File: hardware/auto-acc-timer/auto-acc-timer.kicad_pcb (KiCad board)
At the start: 2 copper layers, 38.1 x 20.3 mm, 12 parts, among them J1 Conn_01x07_Pin, J3 Conn_02x03_Odd_Even, Q1 BRC108, Q2 BSS83P, U1 ATtiny85-20S, U2 MCP1703Ax-330xxDB

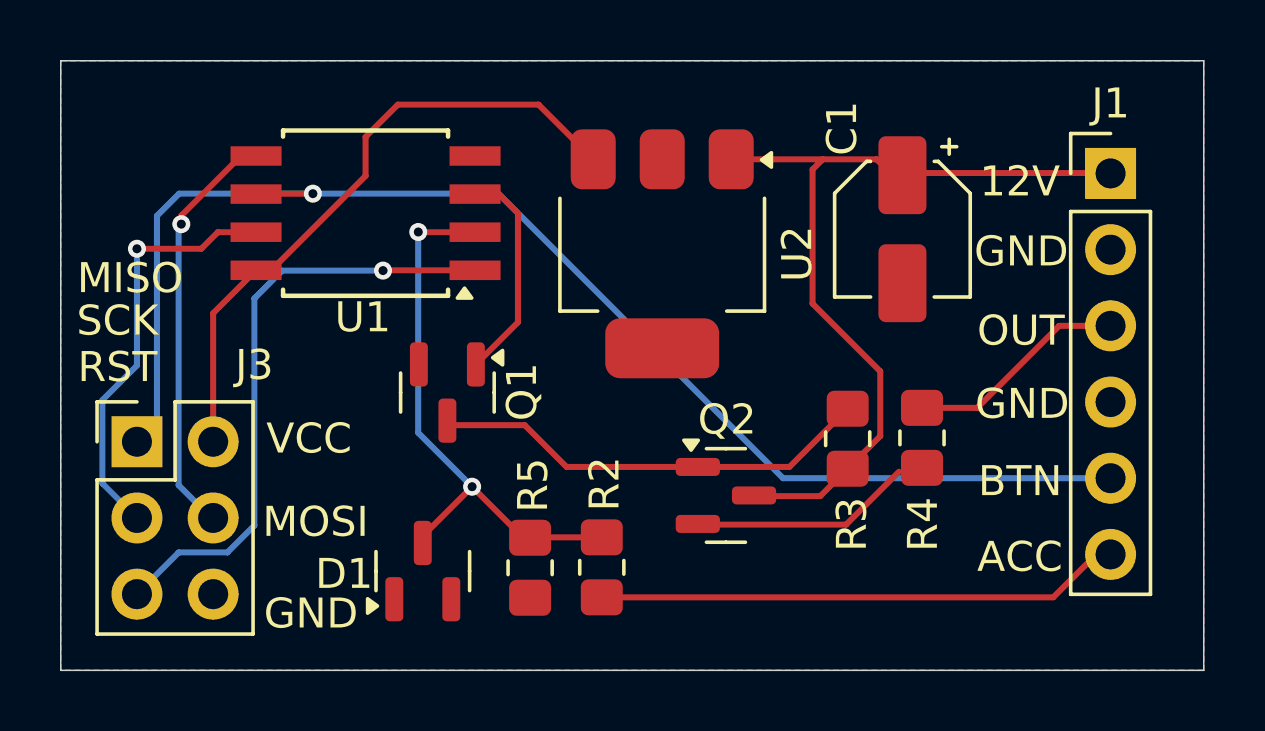
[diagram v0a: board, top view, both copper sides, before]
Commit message: Fix wrong connection of Q2, move to KiCAD v 9
The Q2 FET was connected the wrong way, fix that. and Move to KiCAD
version9
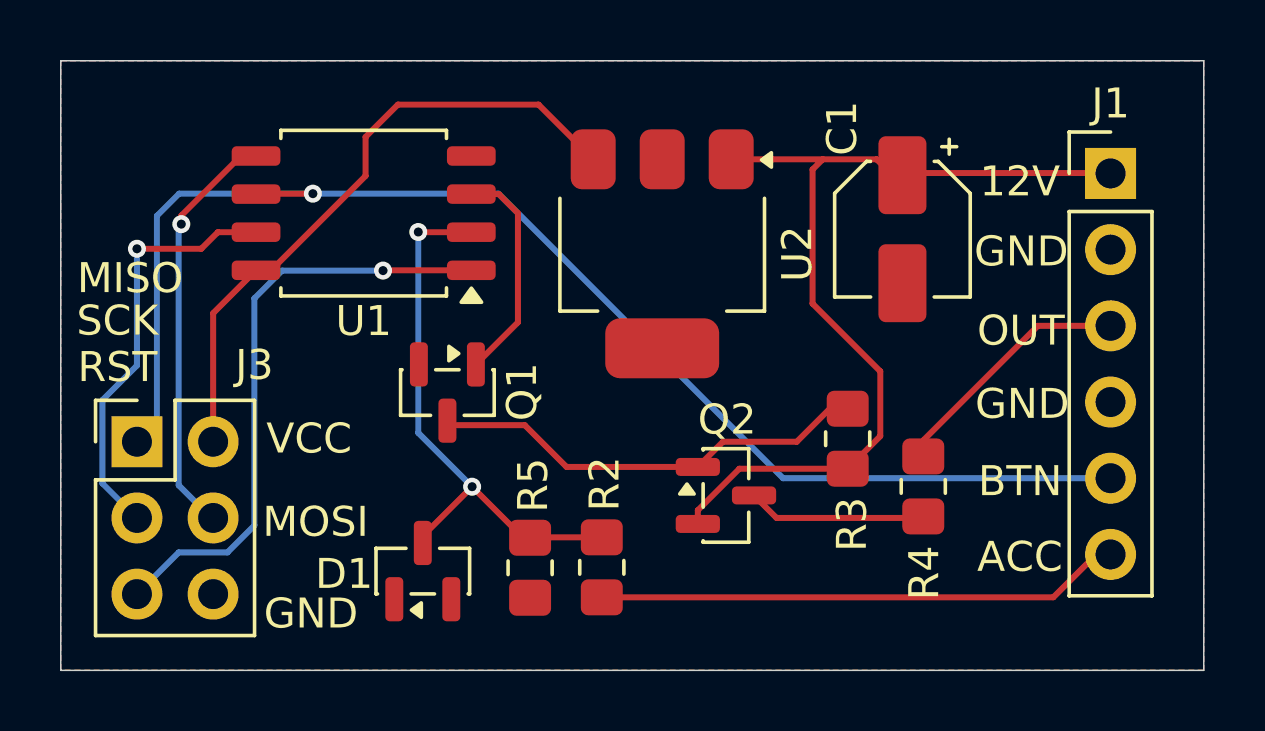
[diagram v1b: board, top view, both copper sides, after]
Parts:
- Q1: value BRC108 -> BCR108
- U1: value ATtiny85-20S -> ATtiny85-20SU; footprint Package_SO:SOIC-8W_5.3x5.3mm_P1.27mm -> Package_SO:SOIC-8_5.3x5.3mm_P1.27mm
- U2: value MCP1703Ax-330xxDB -> MCP1703A-3302EDB
- moved R4 1.62 mm to (143.1, 85.3)
- moved U1 0.06 mm to (124.4, 76.2)
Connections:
- Q2 pad 2: Net-(Q2-S) -> +12V
- Q2 pad 3: +12V -> Net-(Q2-D)
- R4 pad 1: Net-(Q2-S) -> Net-(Q2-D)
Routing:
- net Net-(Q2-S): track 7.44 -> 0.00 mm
- net Net-(Q2-D): track 0.00 -> 6.06 mm
- net +12V: track 28.2 -> 30.7 mm
- net ACC OUT: track 7.42 -> 8.36 mm

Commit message: Rev 2 Hardware
Add capacitor 1uF at 3.3V rail
Add resistor to pull RESET high
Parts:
- added C2: 1uF, Capacitor_SMD:C_0805_2012Metric_Pad1.18x1.45mm_HandSolder, F.Cu at (132.6, 73.2)
- added R1: 100k, Resistor_SMD:R_0805_2012Metric_Pad1.20x1.40mm_HandSolder, F.Cu at (123.1, 80.7)
- moved U2 1.90 mm to (135.4, 79.1)
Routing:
- net 3V3: track 21.4 -> 27.6 mm
- net Net-(J3-Pin_5): track 20.2 -> 23.1 mm

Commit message: Optimize PCB layout
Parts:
- moved C2 1.67 mm to (134.3, 73.1)
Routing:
- net 3V3: track 27.6 -> 28.2 mm
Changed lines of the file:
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@@
 	(footprint "Capacitor_SMD:C_0805_2012Metric_Pad1.18x1.45mm_HandSolder"
 		(layer "F.Cu")
-		(at 132.620663 73.242078)
+		(at 134.284778 73.139357)
 		(descr "Capacitor SMD 0805 (2012 Metric), square (rectangular) end terminal, IPC-7351 nominal with elongated pad for handsoldering. (Body size source: IPC-SM-782 page 76, https://www.pcb-3d.com/wordpress/wp-content/uploads/ipc-sm-782a_amendment_1_and_2.pdf, https://docs.google.com/spreadsheets/d/1BsfQQcO9C6DZCsRaXUlFlo91Tg2WpOkGARC1WS5S8t0/edit?usp=sharing), generated with kicad-footprint-generator")
 		(tags "capacitor handsolder")
@@
 	)
 	(segment
-		(start 125.537907 72.582093)
-		(end 124.46 73.66)
+		(start 131.583163 73.242078)
+		(end 131.301885 72.9608)
 		(width 0.2)
 		(layer "F.Cu")
@@
 	)
 	(segment
-		(start 133.132884 75.970647)
-		(end 133.132884 74.791799)
+		(start 125.159201 72.9608)
+		(end 124.46 73.660001)
+		(width 0.2)
+		(layer "F.Cu")
+		(net 14)
+	)
+	(segment
+		(start 131.301885 72.9608)
+		(end 125.159201 72.9608)
+		(width 0.2)
+		(layer "F.Cu")
+		(net 14)
+	)
+	(segment
+		(start 124.46 74.96)
+		(end 121.315 78.105)
 		(width 0.2)
 		(layer "F.Cu")
@@
 	)
 	(segment
-		(start 131.583163 73.242078)
-		(end 130.923178 72.582093)
-		(width 0.2)
-		(layer "F.Cu")
-		(net 14)
-	)
-	(segment
 		(start 122.112007 80.680369)
 		(end 122.112007 78.902007)
@@
 	)
 	(segment
-		(start 124.46 73.66)
+		(start 133.132884 75.970647)
+		(end 133.132884 73.242078)
+		(width 0.2)
+		(layer "F.Cu")
+		(net 14)
+	)
+	(segment
+		(start 133.132884 73.242078)
+		(end 131.583163 73.242078)
+		(width 0.2)
+		(layer "F.Cu")
+		(net 14)
+	)
+	(segment
+		(start 124.46 73.660001)
 		(end 124.46 74.96)
-		(width 0.2)
-		(layer "F.Cu")
-		(net 14)
-	)
-	(segment
-		(start 133.132884 74.791799)
-		(end 131.583163 73.242078)
 		(width 0.2)
 		(layer "F.Cu")
@@
 	)
 	(segment
-		(start 124.46 74.96)
-		(end 121.315 78.105)
-		(width 0.2)
-		(layer "F.Cu")
-		(net 14)
-	)
-	(segment
 		(start 122.112007 78.902007)
 		(end 121.315 78.105)
 		(width 0.2)
 		(layer "F.Cu")
-		(net 14)
-	)
-	(segment
-		(start 130.923178 72.582093)
-		(end 125.537907 72.582093)
-		(width 0.2)
-		(layer "F.Cu")
